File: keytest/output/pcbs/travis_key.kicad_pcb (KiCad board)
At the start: 2 copper layers, 51.4 x 51.4 mm, 4 parts

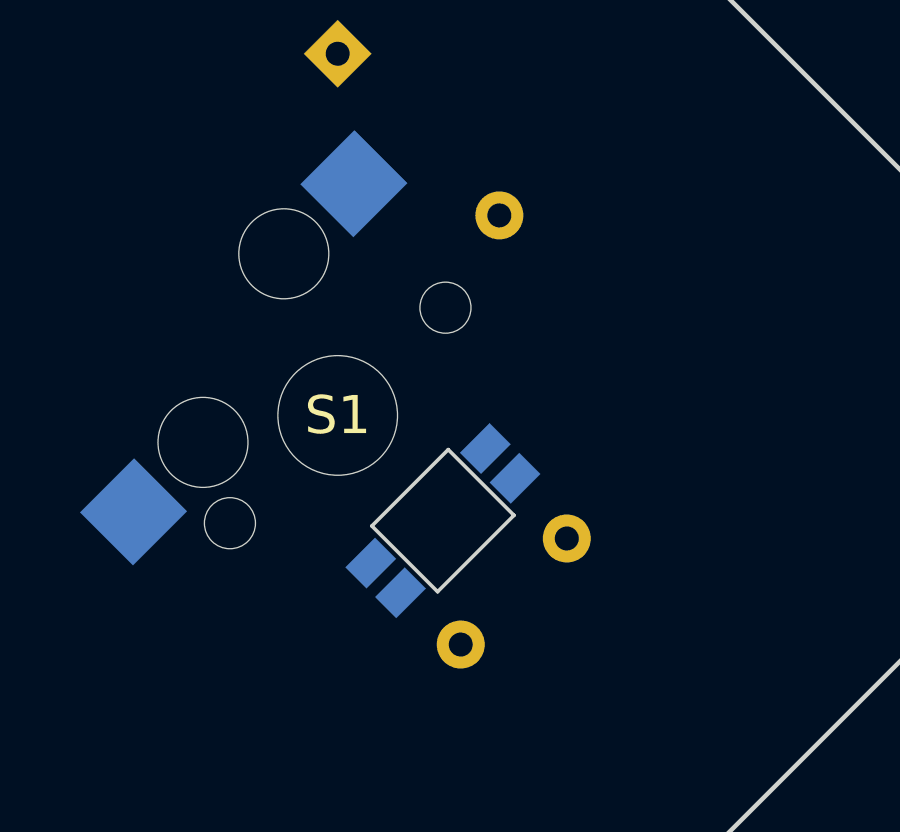
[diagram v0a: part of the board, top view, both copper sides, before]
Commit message: key module functions with traces
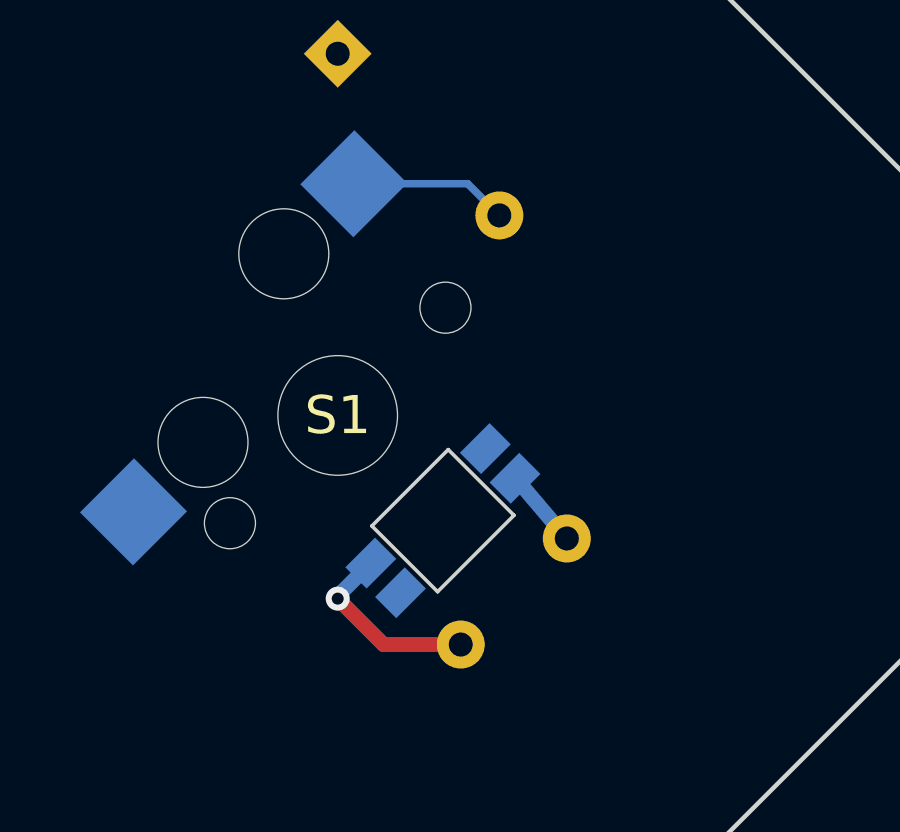
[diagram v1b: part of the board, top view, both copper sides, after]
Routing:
- net GND: track 0.00 -> 6.38 mm, vias 0 -> 1
- net single_A_one: track 0.00 -> 5.29 mm
- net RAW: track 0.00 -> 2.73 mm
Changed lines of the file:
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@@
   )
+)
+(segment
+  (start 104.3332 92.2770)
+  (end 105.3882 93.3320)
+  (width 0.25)
+  (layer "B.Cu")
+  (net 1)
+)
+(segment
+  (start 100.5388 92.2770)
+  (end 104.3332 92.2770)
+  (width 0.25)
+  (layer "B.Cu")
+  (net 1)
+)
+(segment
+  (start 107.6368 104.1012)
+  (end 106.0528 102.2345)
+  (width 0.5)
+  (layer "B.Cu")
+  (net 6)
+)
+(segment
+  (start 105.9114 102.3759)
+  (end 105.9114 102.0930)
+  (width 0.5)
+  (layer "B.Cu")
+  (net 6)
+)
+(segment
+  (start 100.0000 106.1066)
+  (end 101.5302 107.6368)
+  (width 0.5)
+  (layer "F.Cu")
+  (net 7)
+)
+(segment
+  (start 101.5302 107.6368)
+  (end 104.1012 107.6368)
+  (width 0.5)
+  (layer "F.Cu")
+  (net 7)
+)
+(via
+  (at 100.0000 106.1066)
+  (size 0.8)
+  (drill 0.4)
+  (layers "F.Cu" "B.Cu")
+  (net 7)
+)
+(segment
+  (start 101.1031 104.9215)
+  (end 100.0000 106.0245)
+  (width 0.5)
+  (layer "B.Cu")
+  (net 7)
+)
+(segment
+  (start 100.0000 106.0245)
+  (end 100.0000 106.1066)
+  (width 0.5)
+  (layer "B.Cu")
+  (net 7)
 )
             (gr_line (start 97.8786797 124.8194481) (end 75.1805519 102.1213203) (angle 90) (layer Edge.Cuts) (width 0.15))
